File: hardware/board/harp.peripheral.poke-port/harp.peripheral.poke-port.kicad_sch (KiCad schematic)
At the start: 19 parts, among them J1 Conn_01x03_Socket, U1 TPS63060, U2 EE-SX1140, U3 74LVCH2T45DC

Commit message: add 3d models
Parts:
- J1: Link (none) -> https://www.digikey.com/en/products/detail/3m/37203-62B3-00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
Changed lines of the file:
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@@
+			)
+		)
+		(property "Link" "https://www.digikey.com/en/products/detail/3m/37203-62B3-003PL/1642668"
+			(at 21.59 35.56 0)
+			(effects
+				(font
+					(size 1.27 1.27)
+				)
+				(hide yes)
 			)
 		)

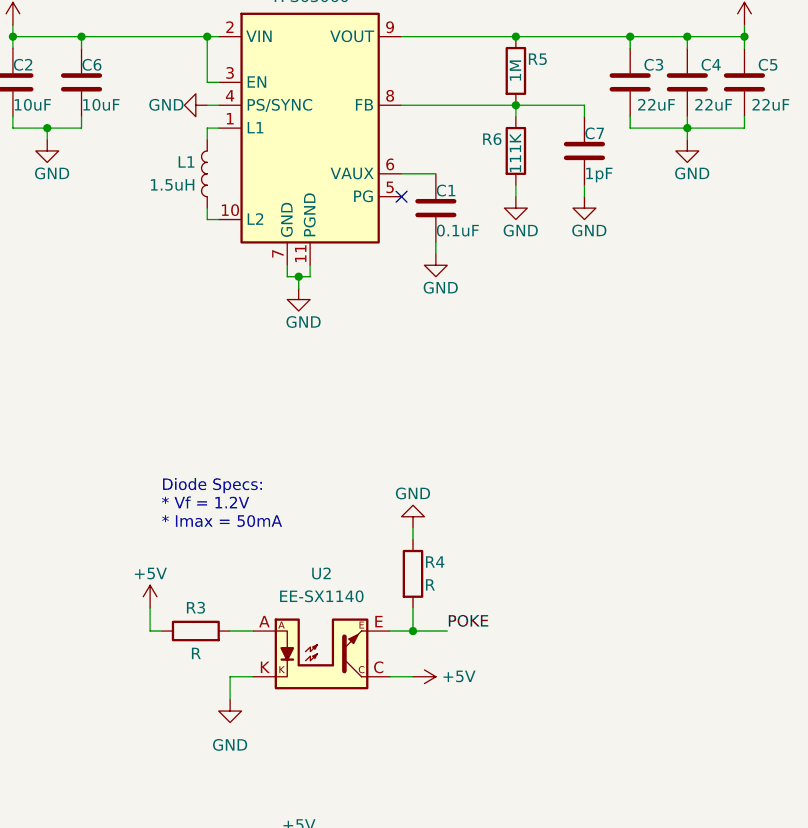
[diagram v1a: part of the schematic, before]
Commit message: update min soldermask bridge to 0.2mm
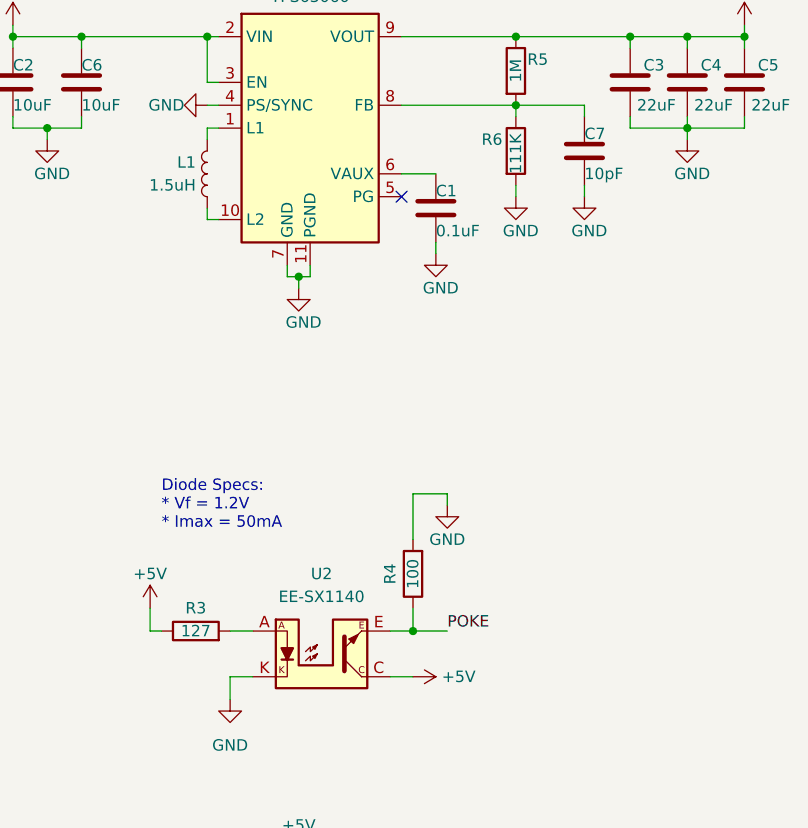
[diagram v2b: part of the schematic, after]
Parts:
- C7: value 1pF -> 10pF; footprint Capacitor_SMD:C_0603_1608Metric -> Capacitor_SMD:C_0402_1005Metric; Link (none) -> https://www.digikey.com/en/products/detail/murata-electroni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; Manufacturer (none) -> Murata Electronics; Manufacturer Number (none) -> GRM1555C1H100JA01D
- L1: footprint kicad-lib:1226AS-H-1R5N=P2 -> kicad-lib:L_Murata_1226AS-H-1R5N=P2
- R3: value R -> 127; Link (none) -> https://www.digikey.com/en/products/detail/yageo/RC0603FR-0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; Manufacturer (none) -> Yageo; Manufacturer Number (none) -> RC0603FR-07127RL
- R4: value R -> 100; Link (none) -> https://www.digikey.com/en/products/detail/yageo/SR0603FR-7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; Manufacturer (none) -> Yageo; Manufacturer Number (none) -> SR0603FR-7T100RL; Notes (none) -> 1/4W; Tolerance (none) -> 1%
- R5: Link (none) -> https://www.digikey.com/en/products/detail/yageo/RC0402FR-0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; Manufacturer (none) -> Yageo; Manufacturer Number (none) -> RC0402FR-071ML
- R6: Link (none) -> https://www.digikey.com/en/products/detail/koa-speer-electr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; Manufacturer (none) -> KOA Speer Electronics, Inc.; Manufacturer Number (none) -> RN73H1ETTP1113F25
- U1: Link (none) -> https://www.digikey.com/en/products/detail/texas-instrument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
- U2: Link (none) -> https://www.digikey.com/en/products/detail/omron-electronic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; Manufacturer (none) -> Omron Electronics Inc-EMC Div; Manufacturer Number (none) -> EE-SX1140
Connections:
- net GND: now also R4.2; no longer R4.1
- net POKE: now also R4.1; no longer R4.2

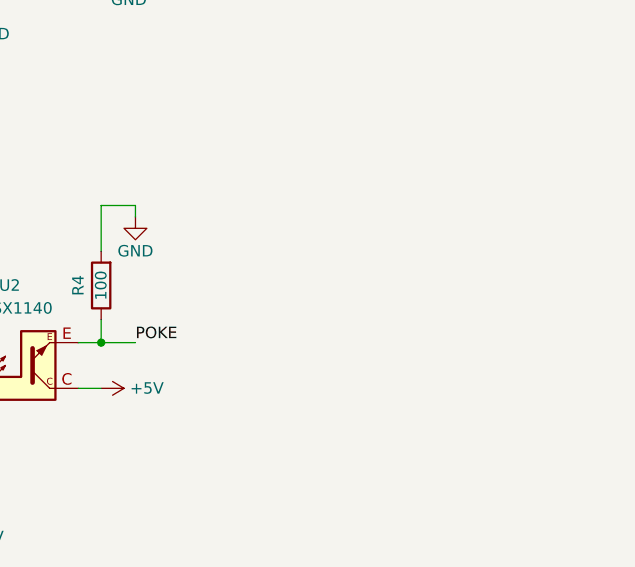
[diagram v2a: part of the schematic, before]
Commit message: add schematic errata note
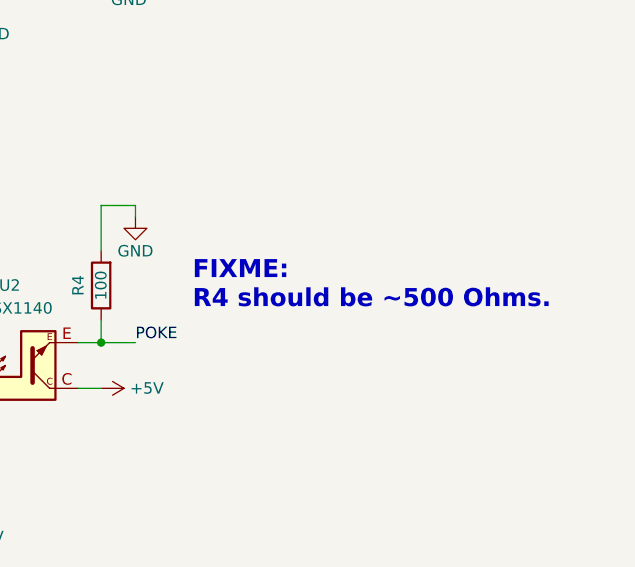
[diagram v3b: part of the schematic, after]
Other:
- note added: "FIXME: R4 should be ~500 Ohms."
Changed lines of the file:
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@@
+		)
+	)
+	(text "FIXME:\nR4 should be ~500 Ohms."
+		(exclude_from_sim no)
+		(at 151.13 85.09 0)
+		(effects
+			(font
+				(size 2 2)
+				(thickness 0.254)
+				(bold yes)
+			)
+			(justify left)
 		)
 	)

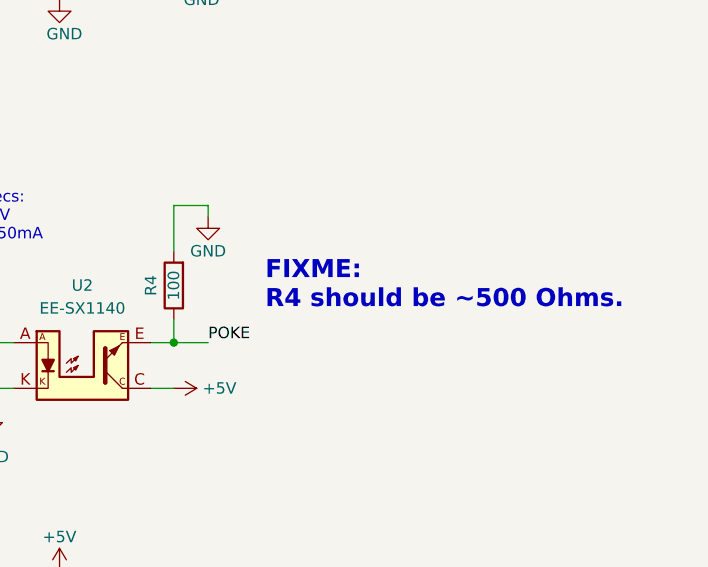
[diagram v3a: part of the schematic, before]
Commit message: update photointerrupter resistor
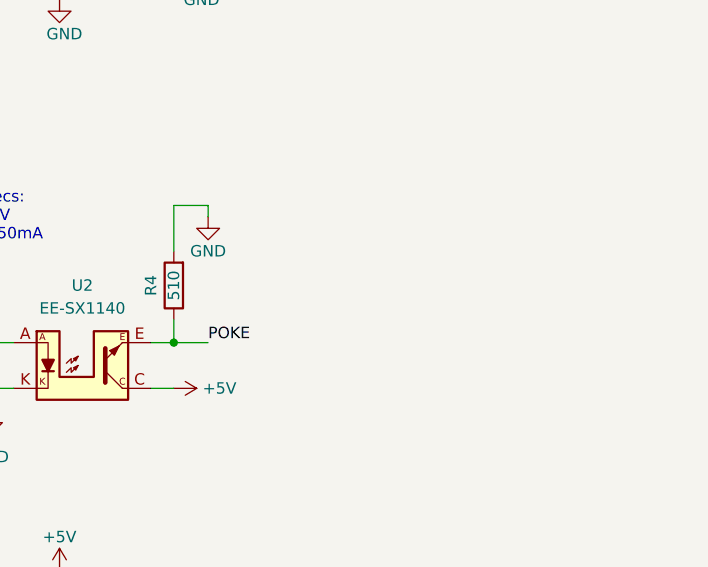
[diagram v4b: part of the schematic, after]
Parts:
- R4: value 100 -> 510; Link https://www.digikey.com/en/products/detail/yageo/SR0603FR-7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 -> https://www.digikey.com/en/products/detail/koa-speer-electr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; Manufacturer Yageo -> KOA Speer Electronics, Inc.; Manufacturer Number SR0603FR-7T100RL -> SG73P1JTTD5100F; Notes 1/4W -> 1/3W
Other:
- note removed: "FIXME: R4 should be ~500 Ohms."
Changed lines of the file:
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@@
-		)
-	)
-	(text "FIXME:\nR4 should be ~500 Ohms."
-		(exclude_from_sim no)
-		(at 151.13 85.09 0)
-		(effects
-			(font
-				(size 2 2)
-				(thickness 0.254)
-				(bold yes)
-			)
-			(justify left)
 		)
 	)
@@
 			)
 		)
-		(property "Value" "100"
+		(property "Value" "510"
 			(at 140.97 85.09 90)
 			(effects
@@
 			)
 		)
-		(property "Datasheet" "https://www.yageo.com/upload/media/product/productsearch/datasheet/rchip/PYu-SR_20105_RoHS_L_10.pdf"
+		(property "Datasheet" "https://www.koaspeer.com/pdfs/SG73P.pdf"
 			(at 140.97 85.09 0)
 			(effects
@@
 			)
 		)
-		(property "Link" "https://www.digikey.com/en/products/detail/yageo/SR0603FR-7T100RL/9373096"
+		(property "Link" "https://www.digikey.com/en/products/detail/koa-speer-electronics-inc/SG73P1JTTD5100F/10188211"
 			(at 140.97 85.09 0)
 			(effects
@@
 			)
 		)
-		(property "Manufacturer" "Yageo"
+		(property "Manufacturer" "KOA Speer Electronics, Inc."
 			(at 140.97 85.09 0)
 			(effects
@@
 			)
 		)
-		(property "Manufacturer Number" "SR0603FR-7T100RL"
+		(property "Manufacturer Number" "SG73P1JTTD5100F"
 			(at 140.97 85.09 0)
 			(effects
@@
 			)
 		)
-		(property "Notes" "1/4W"
+		(property "Notes" "1/3W"
 			(at 140.97 85.09 0)
 			(effects

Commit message: Fixed R4 -> 510ohm
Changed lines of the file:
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@@
 (kicad_sch
-	(version 20231120)
+	(version 20250114)
 	(generator "eeschema")
-	(generator_version "8.0")
+	(generator_version "9.0")
 	(paper "A4")
+	(text "TTL Output\n50Ohm Output Impedance"
+		(exclude_from_sim no)
+		(at 152.4 125.73 0)
+		(effects
+			(font
+				(size 1.27 1.27)
+			)
+			(justify left)
+		)
+	)
+	(text "Input Voltage: 2.5-12V"
+		(exclude_from_sim no)
+		(at 26.035 25.4 0)
+		(effects
+			(font
+				(size 1.27 1.27)
+			)
+		)
+	)
+	(text "Diode Specs:\n* Vf = 1.2V\n* Imax = 50mA"
+		(exclude_from_sim no)
+		(at 113.03 77.47 0)
+		(effects
+			(font
+				(size 1.27 1.27)
+			)
+			(justify left)
+		)
+	)
 	(junction
 		(at 171.45 35.56)
@@
 		)
 	)
-	(text "TTL Output\n50Ohm Output Impedance"
-		(exclude_from_sim no)
-		(at 152.4 125.73 0)
-		(effects
-			(font
-				(size 1.27 1.27)
-			)
-			(justify left)
-		)
-	)
-	(text "Input Voltage: 2.5-12V"
-		(exclude_from_sim no)
-		(at 26.035 25.4 0)
-		(effects
-			(font
-				(size 1.27 1.27)
-			)
-		)
-	)
-	(text "Diode Specs:\n* Vf = 1.2V\n* Imax = 50mA"
-		(exclude_from_sim no)
-		(at 113.03 77.47 0)
-		(effects
-			(font
-				(size 1.27 1.27)
-			)
-			(justify left)
-		)
-	)
 	(label "TTL_POKE"
 		(at 152.4 132.08 0)
-		(fields_autoplaced yes)
 		(effects
 			(font
@@
 	(label "POKE"
 		(at 144.78 91.44 0)
-		(fields_autoplaced yes)
 		(effects
 			(font
@@
 	(label "POKE"
 		(at 115.57 132.08 180)
-		(fields_autoplaced yes)
 		(effects
 			(font
@@
 	(label "TTL_POKE"
 		(at 30.48 33.02 0)
-		(fields_autoplaced yes)
 		(effects
 			(font
@@
 		)
 	)
+	(embedded_fonts no)
 )
